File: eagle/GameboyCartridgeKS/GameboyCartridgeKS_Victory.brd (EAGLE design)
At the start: 49.3 x 48 mm, 17 parts, among them IC1 AT49F040J

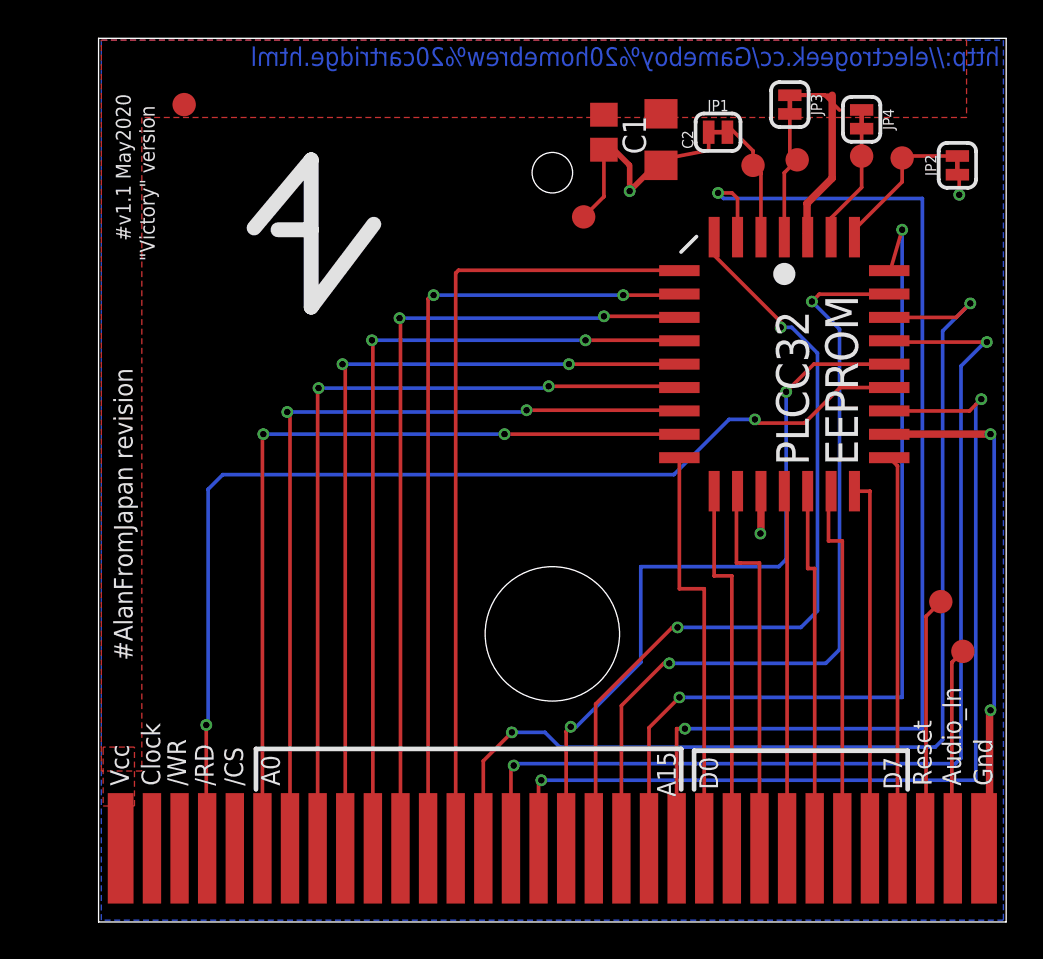
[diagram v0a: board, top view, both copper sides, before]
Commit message: New Pigman logo, Victory GB cartridge in last round of review
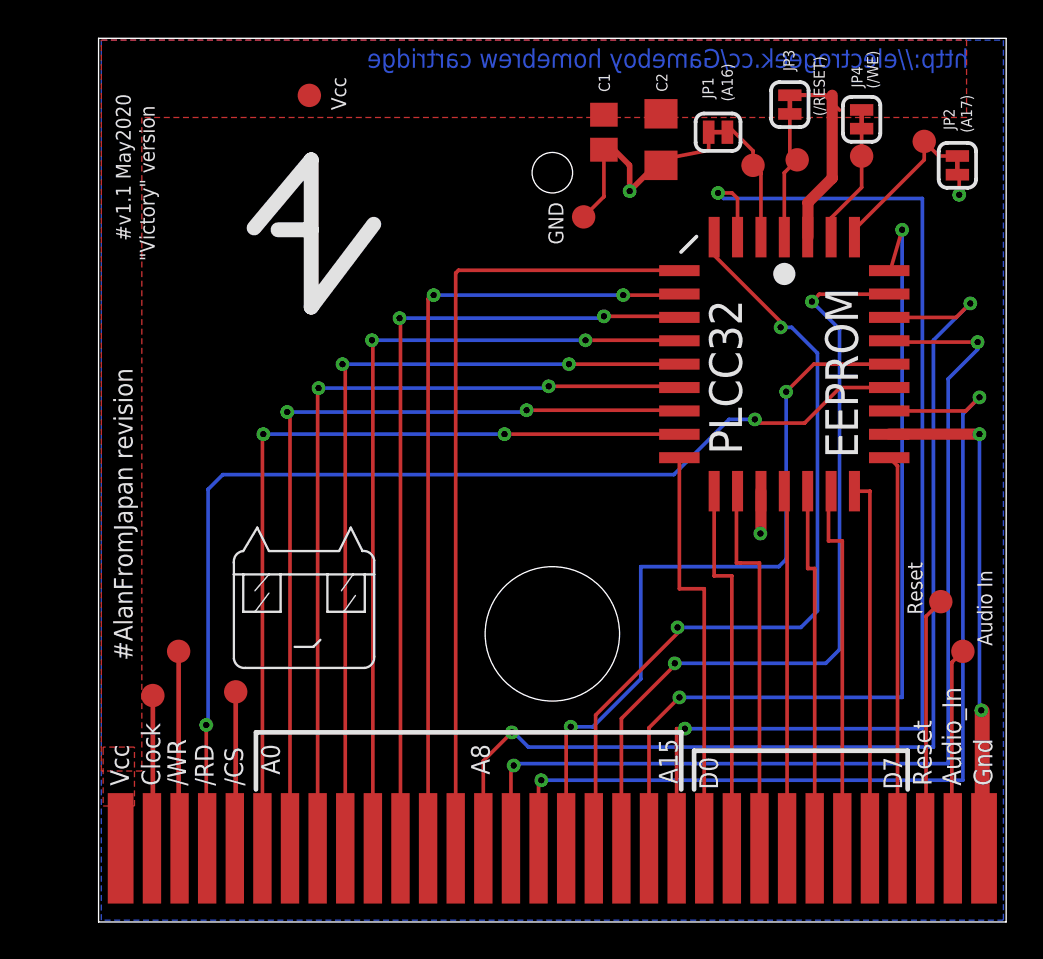
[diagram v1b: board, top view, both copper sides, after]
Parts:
- added TP10, TP11, TP9: TEST-POINT3X5, SparkFun-Connectors:PAD.03X.05
- added U$3: (no value), kalshagar-images:PIGMAN1
- moved TP6 6.82 mm to (12.3, 44.9)
- moved TP3 1.50 mm to (45.7, 42.4)
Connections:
- new net N$2: TP11.P$1, U$1.2
- net 3: now also TP9.P$1
- net 5: now also TP10.P$1
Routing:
- net 3: track 0.00 -> 10.7 mm
- net 5: track 0.00 -> 8.52 mm
- net N$2: track 0.00 -> 8.32 mm
- net 15: track 57.6 -> 56.6 mm
- net GND: track 45.0 -> 44.2 mm
- net 17: track 40.5 -> 41.1 mm
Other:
- board text added: "(/RESET)"
- board text added: "(/WE)"
- board text added: "(A16)"
- board text added: "(A17)"
- board text added: "A8"
- board text added: "Audio In"
- board text added: "EEPROM"
- board text added: "GND"
- board text added: "PLCC32"
- board text added: "http://electrogeek.cc/Gameboy homebrew cartridge"
- board text removed: "PLCC32 EEPROM"
- board text removed: "http://electrogeek.cc/Gameboy%20homebrew%20cartridge.html"

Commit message: Board GB Victory sent to prod.
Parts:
- added JP5: JUMPER-SMT_3_1-NC_TRACE_SILK, SparkFun-Jumpers:SMT-JUMPER_3_1-NC_TRACE_SILK
- added TP12: TEST-POINT3X5, SparkFun-Connectors:PAD.03X.05
- moved TP11 5.56 mm to (4.60, 17.8)
- moved U$3 2.41 mm to (8.00, 16.2)
- moved TP2 1.22 mm to (36.6, 42.3)
- moved TP4 0.71 mm to (38.9, 42.1)
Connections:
- new net N$3: IC1.3, JP5.2, TP12.P$1
- net 21: now also JP5.1; no longer IC1.3
- net GND: now also JP5.3
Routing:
- net VDD: track 14.1 -> 64.5 mm
- net N$3: track 0.00 -> 22.2 mm
- net 21: track 63.2 -> 82.1 mm
- net GND: track 44.2 -> 50.7 mm
- net N$2: track 8.32 -> 14.2 mm
- net 14: track 59.8 -> 61.5 mm
- net 20: track 49.1 -> 50.7 mm
- net 19: track 44.5 -> 45.4 mm
- net 17: track 41.1 -> 41.9 mm
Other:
- board text added: "(A15)"
- board text added: "*1.0-1.2 mm thickness"
- board text added: "32kB"
- board text added: "JLCJLCJLCJLC"
